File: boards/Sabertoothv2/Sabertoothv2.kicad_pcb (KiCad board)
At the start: 2 copper layers, 45.6 x 45.6 mm, 40 parts, among them J1 Screw_Terminal_01x04, J2 Screw_Terminal_01x04, J4 Conn_01x04_Pin, J5 Conn_01x04_Pin, Q1 NMOS, Q2 NMOS, Q3 NMOS, Q4 NMOS, U1 LM2104, U2 LM2104, U4 74LVC1GU04DRL

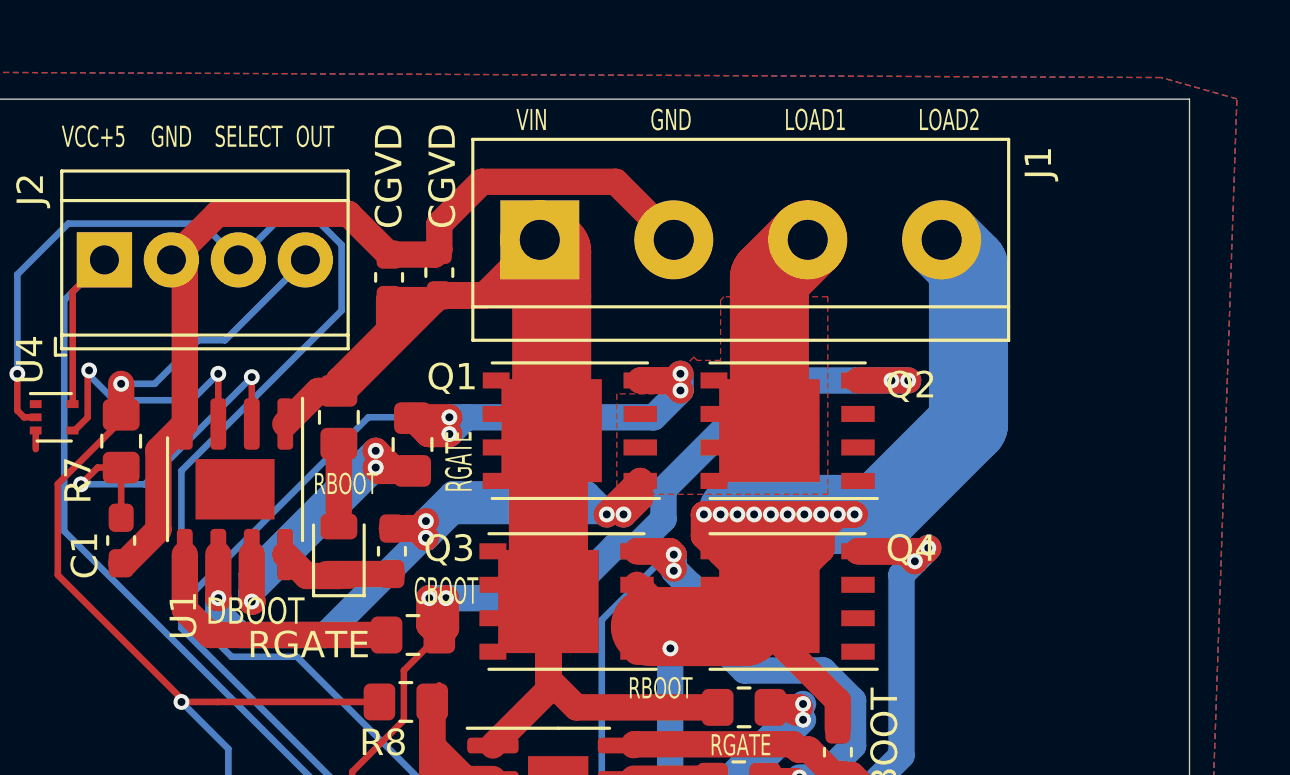
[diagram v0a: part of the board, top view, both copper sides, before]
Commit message: minor changes on front silkscreen and added a smaller iris logo
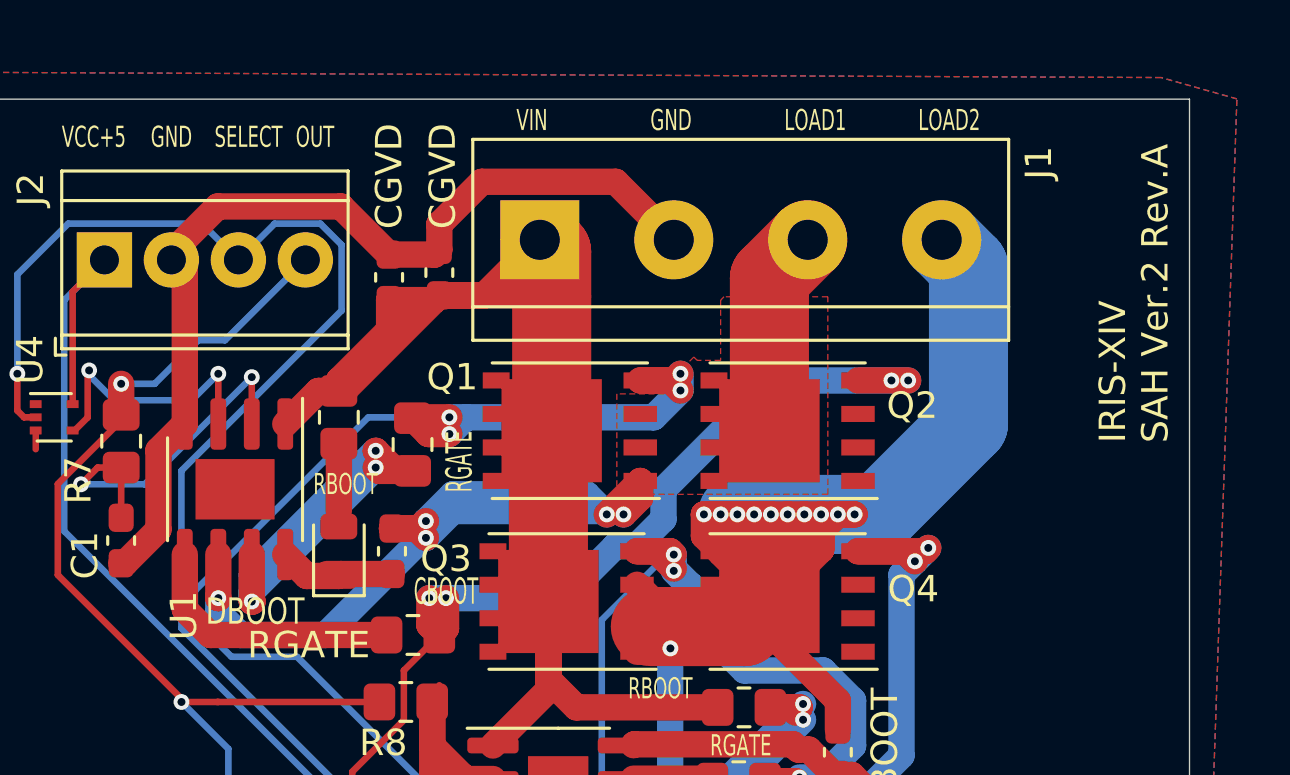
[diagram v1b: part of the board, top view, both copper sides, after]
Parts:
- removed the G*** at (71.1, 40.0)
- added G***: LOGO, Custom_Silkscreen_and_memes:IRIS_logo_smaller, B.Cu at (91.6, 37.5)
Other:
- board text added: "IRIS-XIV SAH Ver.2 Rev.A"
- board text added: "IRIS-XIV SAH Ver.2 Rev.A Buffet Lee, Emily Lory, Joseph Hanger Caroline Chang, Ethan Chang, Jiho Choi, Nathan Colunga, Henry Lin, Ben Saarva, Jashan Virdi, Jakub Wojdyla"
- board text removed: "Nathan Colunga Lee Buffett Emily Lory Joseph Hanger"

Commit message: update name
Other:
- board text added: "IRIS-XIV SAH Ver.2 Rev.A Buffett Lee, Emily Lory, Joseph Hanger Caroline Chang, Ethan Chang, Jiho Choi, Nathan Colunga, Henry Lin, Ben Saarva, Jashan Virdi, Jakub Wojdyla"
- board text removed: "IRIS-XIV SAH Ver.2 Rev.A Buffet Lee, Emily Lory, Joseph Hanger Caroline Chang, Ethan Chang, Jiho Choi, Nathan Colunga, Henry Lin, Ben Saarva, Jashan Virdi, Jakub Wojdyla"
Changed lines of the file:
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@@
     (effects (font (size 1 1) (thickness 0.25) bold) (justify left bottom mirror))
   )
-  (gr_text "IRIS-XIV\nSAH Ver.2 Rev.A\nBuffet Lee, Emily Lory, Joseph Hanger\nCaroline Chang, Ethan Chang, Jiho Choi,\nNathan Colunga, Henry Lin, Ben Saarva, \nJashan Virdi, Jakub Wojdyla" (at 86.49 63.45) (layer "B.SilkS")
+  (gr_text "IRIS-XIV\nSAH Ver.2 Rev.A\nBuffett Lee, Emily Lory, Joseph Hanger\nCaroline Chang, Ethan Chang, Jiho Choi,\nNathan Colunga, Henry Lin, Ben Saarva, \nJashan Virdi, Jakub Wojdyla" (at 86.49 63.45) (layer "B.SilkS")
     (effects (font (size 1 1) (thickness 0.153)) (justify left bottom mirror))
   )

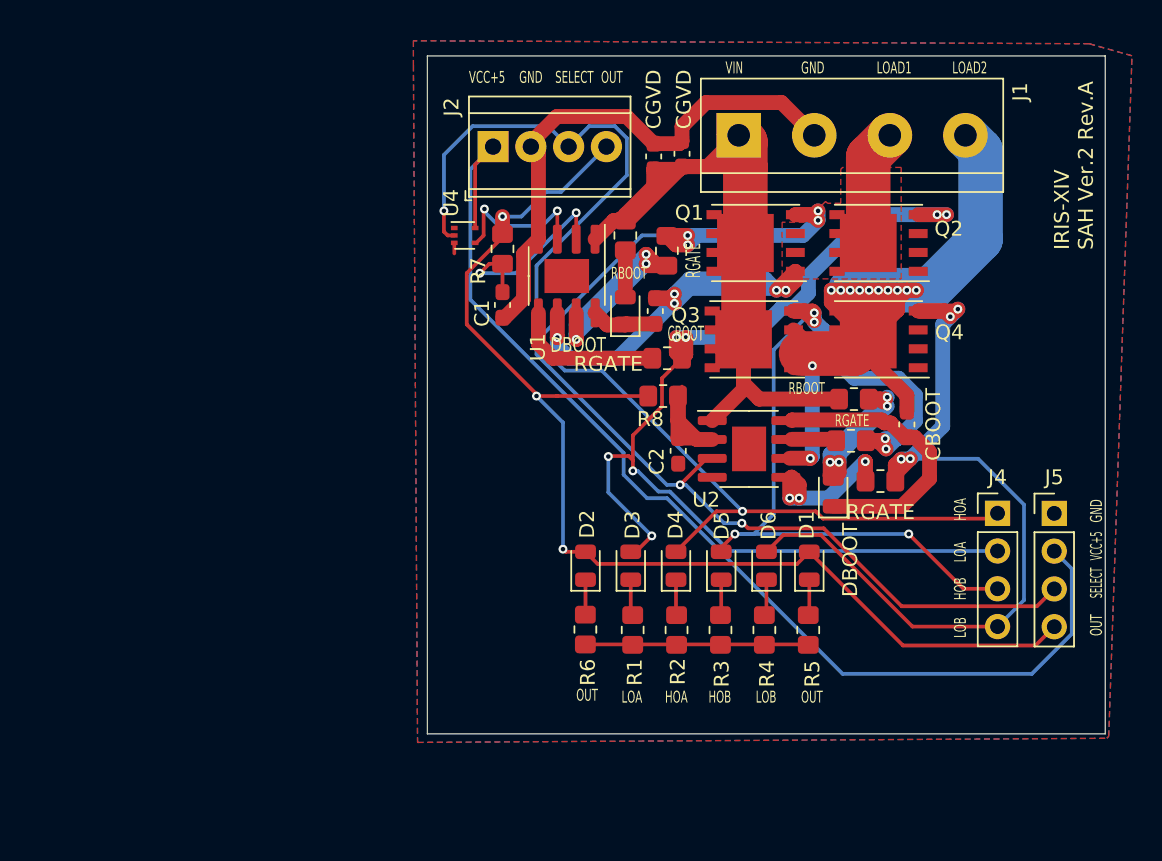
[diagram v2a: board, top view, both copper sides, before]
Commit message: redesigned everything because look better
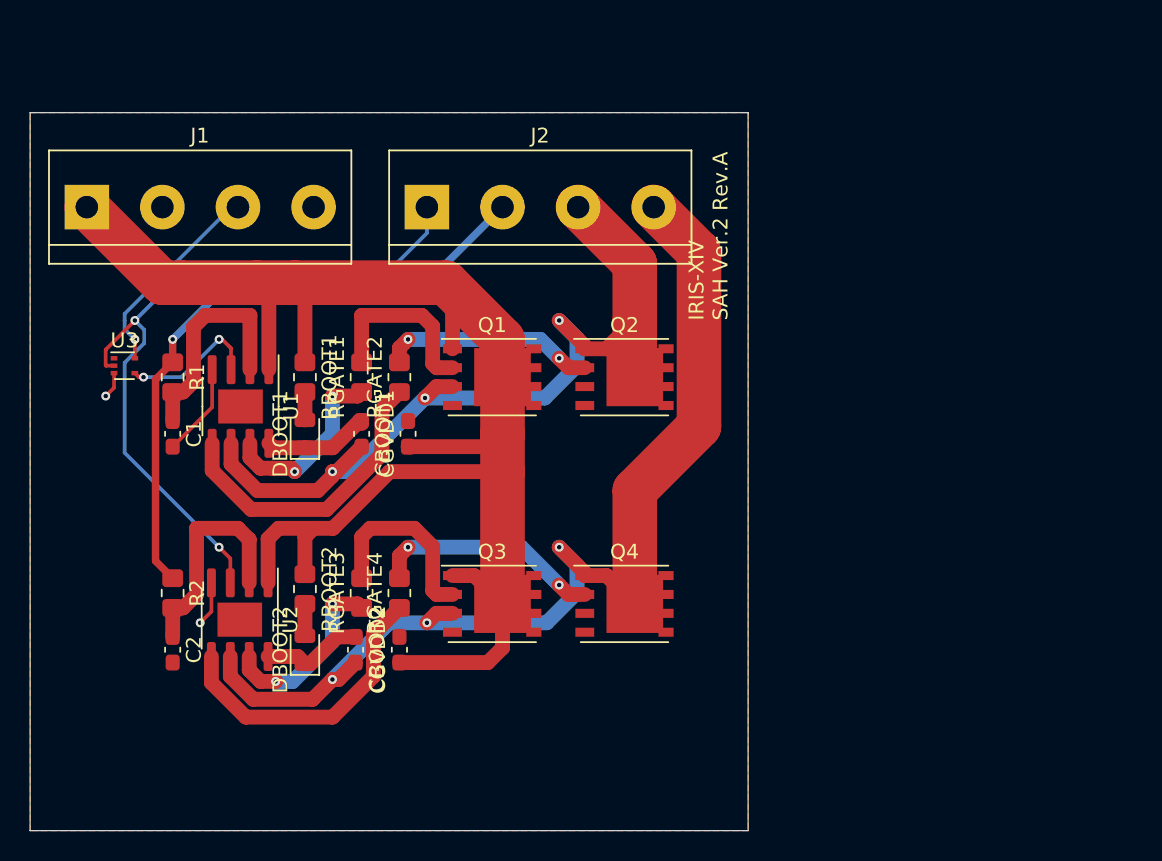
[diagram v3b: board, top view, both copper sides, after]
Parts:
- removed CBOOT (x2): 100nF, Capacitor_SMD:C_0603_1608Metric_Pad1.08x0.95mm_HandSolder
- removed CGVD (x2): 1uF, Capacitor_SMD:C_0603_1608Metric_Pad1.08x0.95mm_HandSolder
- removed D1, D2, D3, D4, D5, D6: LED, LED_SMD:LED_0805_2012Metric
- removed DBOOT (x2): 1V, Diode_SMD:D_0805_2012Metric
- removed J4, J5: Conn_01x04_Pin, Connector_PinHeader_2.54mm:PinHeader_1x04_P2.54mm_Vertical
- removed R3, R4: 1200R, Resistor_SMD:R_0805_2012Metric_Pad1.20x1.40mm_HandSolder
- removed R5, R6: 300R, Resistor_SMD:R_0805_2012Metric_Pad1.20x1.40mm_HandSolder
- removed R7, R8: 50R, Resistor_SMD:R_0805_2012Metric_Pad1.20x1.40mm_HandSolder
- removed RBOOT (x2), RGATE (x4): 2.2R, Resistor_SMD:R_0805_2012Metric_Pad1.20x1.40mm_HandSolder
- removed U4: 74LVC1GU04DRL, Package_TO_SOT_SMD:SOT-553
- added CBOOT1: 100nF, Capacitor_SMD:C_0603_1608Metric_Pad1.08x0.95mm_HandSolder, F.Cu at (46.4, 45.7)
- added CBOOT2: 100nF, Capacitor_SMD:C_0603_1608Metric_Pad1.08x0.95mm_HandSolder, F.Cu at (46.0, 60.2)
- added CGVDD1: 1uF, Capacitor_SMD:C_0603_1608Metric_Pad1.08x0.95mm_HandSolder, F.Cu at (49.5, 45.7)
- added CGVDD2: 1uF, Capacitor_SMD:C_0603_1608Metric_Pad1.08x0.95mm_HandSolder, F.Cu at (49.0, 60.2)
- added DBOOT1: 1V, Diode_SMD:D_0805_2012Metric, F.Cu at (42.6, 45.7)
- added DBOOT2: 1V, Diode_SMD:D_0805_2012Metric, F.Cu at (42.6, 60.2)
- added RBOOT1: 2.2R, Resistor_SMD:R_0805_2012Metric_Pad1.20x1.40mm_HandSolder, F.Cu at (42.6, 41.9)
- added RBOOT2: 2.2R, Resistor_SMD:R_0805_2012Metric_Pad1.20x1.40mm_HandSolder, F.Cu at (42.6, 56.1)
- added RGATE1: 2.2R, Resistor_SMD:R_0805_2012Metric_Pad1.20x1.40mm_HandSolder, F.Cu at (46.4, 41.9)
- added RGATE2: 2.2R, Resistor_SMD:R_0805_2012Metric_Pad1.20x1.40mm_HandSolder, F.Cu at (49.0, 41.9)
- added RGATE3: 2.2R, Resistor_SMD:R_0805_2012Metric_Pad1.20x1.40mm_HandSolder, F.Cu at (46.4, 56.4)
- added RGATE4: 2.2R, Resistor_SMD:R_0805_2012Metric_Pad1.20x1.40mm_HandSolder, F.Cu at (49.0, 56.4)
- added U3: 74LVC1GU04DRL, Package_TO_SOT_SMD:SOT-553, F.Cu at (30.5, 41.1)
- J2: footprint TerminalBlock_TE-Connectivity:TerminalBlock_TE_282834-4_1x04_P2.54mm_Horizontal -> TerminalBlock:TerminalBlock_bornier-4_P5.08mm
- R1, R2: value 1200R -> 50R
- moved J1 44.1 mm to (27.9, 30.5)
- moved C2 36.5 mm to (33.7, 60.2)
- moved U2 36.1 mm to (38.2, 58.2), turned to -90 degrees
- moved R1 35.3 mm to (33.7, 41.9), turned to -90 degrees
- moved R2 34.0 mm to (33.7, 56.4), turned to -90 degrees
- moved G*** 32.9 mm to (67.3, 59.7)
- moved Q3 25.0 mm to (55.2, 57.1), turned to 0 degrees
- moved Q4 24.6 mm to (64.1, 57.1), turned to 0 degrees
- moved C1 23.8 mm to (33.7, 45.7)
- moved U1 23.6 mm to (38.3, 43.9)
- moved Q1 19.9 mm to (55.2, 41.9), turned to 0 degrees
- moved Q2 19.3 mm to (64.1, 41.9), turned to 0 degrees
- moved J2 6.02 mm to (50.8, 30.5)
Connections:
- J1 pad 1: VIN -> VIN+12
- J1 pad 3: LOAD1 -> VIN+5
- J1 pad 4: LOAD2 -> GND
- J2 pad 1: VCC+5 -> SELECT
- J2 pad 2: GND -> PWM
- J2 pad 3: SELECT -> LOAD1
- J2 pad 4: OUT -> LOAD2
- Q1 pad 1: VIN -> VIN+12
- Q3 pad 1: VIN -> VIN+12
- Q3 pad 2: HOB -> HOA
- Q4 pad 2: LOB -> LOA
- R1 pad 1: GND -> PWM
- R1 pad 2: Net-(D3-K) -> Net-(U1-IN)
- R2 pad 1: GND -> PWM
- R2 pad 2: Net-(D4-K) -> Net-(U2-IN)
- U1 pad 1: VIN -> VIN+12
- U2 pad 1: VIN -> VIN+12
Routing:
- net VIN+12: track 0.00 -> 112.5 mm
- net OUT: track 79.6 -> 0.00 mm, vias 3 -> 0
- net VCC+5: track 75.7 -> 0.00 mm
- net HOB: track 61.5 -> 0.00 mm, vias 6 -> 0
- net LOB: track 57.0 -> 0.00 mm, vias 4 -> 0
- net VIN: track 51.1 -> 0.00 mm
- net HOA: track 71.5 -> 24.9 mm, vias 5 -> 0
- net LOA: track 73.3 -> 30.0 mm, vias 7 -> 4
- net PWM: track 0.00 -> 42.9 mm, vias 0 -> 1
- net GND: track 51.9 -> 11.0 mm, vias 0 -> 2
- net SELECT: track 82.9 -> 49.6 mm, vias 3 -> 2
- net LOAD2: track 95.3 -> 72.3 mm, vias 12 -> 3
- net LOAD1: track 42.7 -> 57.4 mm, vias 5 -> 3
- net VIN+5: track 0.00 -> 13.9 mm, vias 0 -> 1
- net Net-(DBOOT2-A): track 15.7 -> 2.14 mm, vias 4 -> 0
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- removed copper zone on B.Cu, net GND
- removed copper zone on F.Cu, net LOAD1
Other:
- board size 45.6 x 45.6 mm -> 48.3 x 48.3 mm
- board text removed: "GND"
- board text removed: "HOA"
- board text removed: "HOB"
- board text removed: "LOA"
- board text removed: "LOAD1"
- board text removed: "LOAD2"
- board text removed: "LOB"
- board text removed: "OUT"
- board text removed: "SELECT"
- board text removed: "VCC+5"
- board text removed: "VIN"

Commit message: added labels for inputs
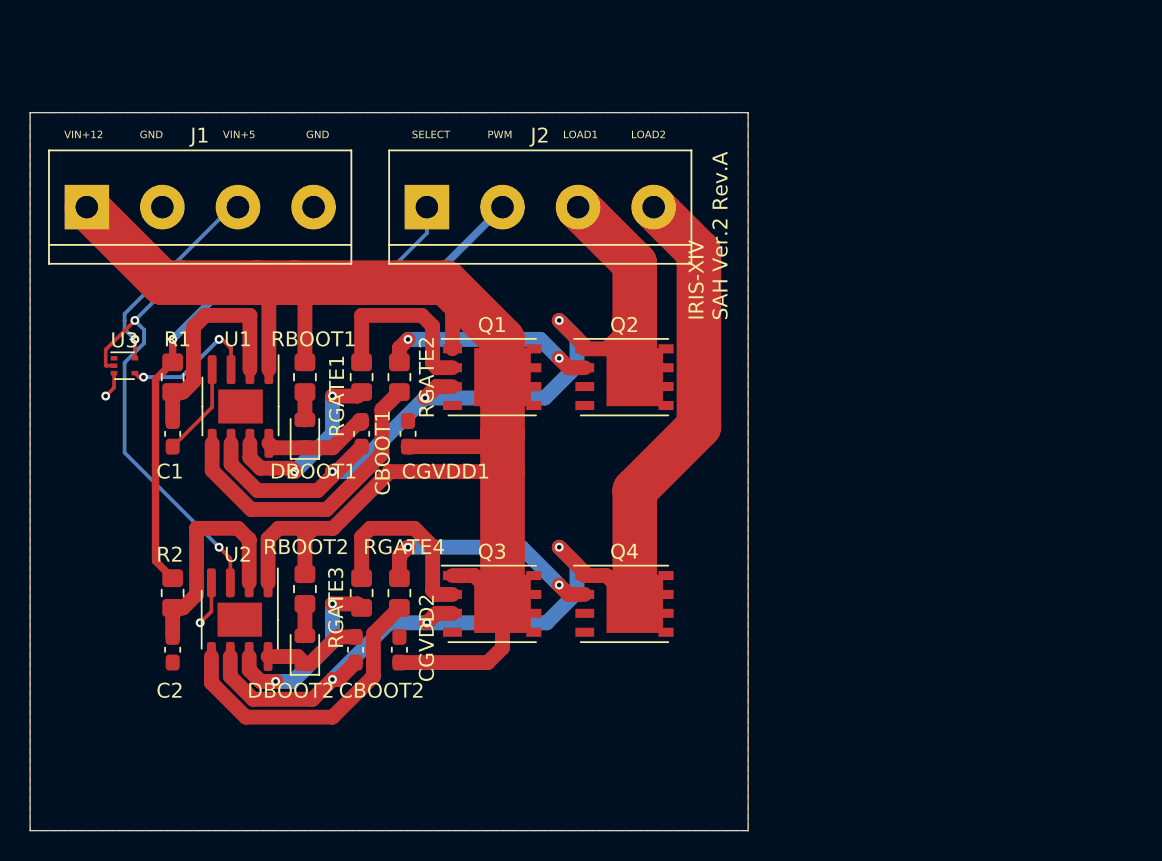
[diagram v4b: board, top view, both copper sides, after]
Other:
- board text added: "GND"
- board text added: "LOAD1"
- board text added: "LOAD2"
- board text added: "PWM"
- board text added: "SELECT"
- board text added: "VIN+12"
- board text added: "VIN+5"
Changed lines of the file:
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@@
     (property "ki_keywords" "cap capacitor")
     (attr smd)
-    (fp_text reference "C1" (at 0 -1.43 90) (layer "F.SilkS")
+    (fp_text reference "C1" (at 2.54 0.182 -180) (layer "F.SilkS")
         (effects (font (size 1 1) (thickness 0.15)))
     )
@@
     (property "ki_keywords" "cap capacitor")
     (attr smd)
-    (fp_text reference "CBOOT1" (at 0 -1.43 90) (layer "F.SilkS")
+    (fp_text reference "CBOOT1" (at 1.27 -1.43 90) (layer "F.SilkS")
         (effects (font (size 1 1) (thickness 0.15)))
     )
@@
     (property "ki_keywords" "driver rs485 rs422 differential")
     (attr smd)
-    (fp_text reference "U2" (at 0 -3.4 90) (layer "F.SilkS")
+    (fp_text reference "U2" (at -4.362 0.12 -180) (layer "F.SilkS")
         (effects (font (size 1 1) (thickness 0.15)))
     )
@@
     (property "ki_keywords" "R res resistor")
     (attr smd)
-    (fp_text reference "RGATE2" (at 0 -1.65 90) (layer "F.SilkS")
+    (fp_text reference "RGATE2" (at 0 1.85 270) (layer "F.SilkS")
         (effects (font (size 1 1) (thickness 0.15)))
     )
@@
     (property "ki_keywords" "R res resistor")
     (attr smd)
-    (fp_text reference "RGATE4" (at 0 -1.65 90) (layer "F.SilkS")
+    (fp_text reference "RGATE4" (at 3.08 0.326 180) (layer "F.SilkS")
         (effects (font (size 1 1) (thickness 0.15)))
     )
@@
     (property "ki_keywords" "diode")
     (attr smd)
-    (fp_text reference "DBOOT2" (at 0 -1.65 90) (layer "F.SilkS")
+    (fp_text reference "DBOOT2" (at -2.762 -0.944 180) (layer "F.SilkS")
         (effects (font (size 1 1) (thickness 0.15)))
     )
@@
     (property "ki_keywords" "R res resistor")
     (attr smd)
-    (fp_text reference "RGATE3" (at 0 -1.65 90) (layer "F.SilkS")
+    (fp_text reference "RGATE3" (at -0.984 -1.706 90) (layer "F.SilkS")
         (effects (font (size 1 1) (thickness 0.15)))
     )
@@
     (property "ki_keywords" "cap capacitor")
     (attr smd)
-    (fp_text reference "CBOOT2" (at 0 -1.43 90) (layer "F.SilkS")
+    (fp_text reference "CBOOT2" (at 2.762 -1.7495 -180) (layer "F.SilkS")
         (effects (font (size 1 1) (thickness 0.15)))
     )
@@
     (property "ki_keywords" "R res resistor")
     (attr smd)
-    (fp_text reference "RBOOT1" (at 0 -1.65 90) (layer "F.SilkS")
+    (fp_text reference "RBOOT1" (at -2.54 -0.58 -180) (layer "F.SilkS")
         (effects (font (size 1 1) (thickness 0.15)))
     )
@@
     (property "ki_keywords" "cap capacitor")
     (attr smd)
-    (fp_text reference "CGVDD1" (at 0 -1.43 90) (layer "F.SilkS")
+    (fp_text reference "CGVDD1" (at -2.54 2.54 180) (layer "F.SilkS")
         (effects (font (size 1 1) (thickness 0.15)))
     )
@@
     (property "ki_keywords" "cap capacitor")
     (attr smd)
-    (fp_text reference "CGVDD2" (at 0 -1.43 90) (layer "F.SilkS")
+    (fp_text reference "CGVDD2" (at 0.794 1.85 90) (layer "F.SilkS")
         (effects (font (size 1 1) (thickness 0.15)))
     )
@@
     (property "ki_keywords" "R res resistor")
     (attr smd)
-    (fp_text reference "R2" (at 0 -1.65 90) (layer "F.SilkS")
+    (fp_text reference "R2" (at -2.572 0.182 -180) (layer "F.SilkS")
         (effects (font (size 1 1) (thickness 0.15)))
     )
@@
     (property "ki_keywords" "diode")
     (attr smd)
-    (fp_text reference "DBOOT1" (at 0 -1.65 90) (layer "F.SilkS")
+    (fp_text reference "DBOOT1" (at -2.54 0.58 180) (layer "F.SilkS")
         (effects (font (size 1 1) (thickness 0.15)))
     )
@@
     (property "ki_keywords" "R res resistor")
     (attr smd)
-    (fp_text reference "RGATE1" (at 0 -1.65 90) (layer "F.SilkS")
+    (fp_text reference "RGATE1" (at -1.27 -1.65 90) (layer "F.SilkS")
         (effects (font (size 1 1) (thickness 0.15)))
     )
@@
     (property "ki_keywords" "R res resistor")
     (attr smd)
-    (fp_text reference "RBOOT2" (at 0 -1.65 90) (layer "F.SilkS")
+    (fp_text reference "RBOOT2" (at -2.81 -0.072 -180) (layer "F.SilkS")
         (effects (font (size 1 1) (thickness 0.15)))
     )
@@
     (property "ki_keywords" "driver rs485 rs422 differential")
     (attr smd)
-    (fp_text reference "U1" (at 0 -3.4 90) (layer "F.SilkS")
+    (fp_text reference "U1" (at -4.51 0.17 -180) (layer "F.SilkS")
         (effects (font (size 1 1) (thickness 0.15)))
     )
@@
     (property "ki_keywords" "R res resistor")
     (attr smd)
-    (fp_text reference "R1" (at 0 -1.65 90) (layer "F.SilkS")
+    (fp_text reference "R1" (at -2.54 -0.326 -180) (layer "F.SilkS")
         (effects (font (size 1 1) (thickness 0.15)))
     )
@@
     (property "ki_keywords" "cap capacitor")
     (attr smd)
-    (fp_text reference "C2" (at 0 -1.43 90) (layer "F.SilkS")
+    (fp_text reference "C2" (at 2.762 0.182 -180) (layer "F.SilkS")
         (effects (font (size 1 1) (thickness 0.15)))
     )
@@
     (effects (font (size 1 1) (thickness 0.153)) (justify left bottom mirror))
   )
+  (gr_text "LOAD1" (at 59.944 25.908) (layer "F.SilkS")
+    (effects (font (size 0.5 0.5) (thickness 0.1)) (justify left bottom))
+  )
+  (gr_text "SELECT" (at 49.784 25.908) (layer "F.SilkS")
+    (effects (font (size 0.5 0.5) (thickness 0.1)) (justify left bottom))
+  )
   (gr_text "IRIS-XIV\nSAH Ver.2 Rev.A" (at 71.12 38.1 90) (layer "F.SilkS")
     (effects (font (size 1 1) (thickness 0.153)) (justify left bottom))
   )
+  (gr_text "VIN+5" (at 37.084 25.908) (layer "F.SilkS")
+    (effects (font (size 0.5 0.5) (thickness 0.1)) (justify left bottom))
+  )
+  (gr_text "GND" (at 31.496 25.908) (layer "F.SilkS")
+    (effects (font (size 0.5 0.5) (thickness 0.1)) (justify left bottom))
+  )
+  (gr_text "VIN+12" (at 26.416 25.908) (layer "F.SilkS")
+    (effects (font (size 0.5 0.5) (thickness 0.1)) (justify left bottom))
+  )
+  (gr_text "LOAD2" (at 64.516 25.908) (layer "F.SilkS")
+    (effects (font (size 0.5 0.5) (thickness 0.1)) (justify left bottom))
+  )
+  (gr_text "PWM" (at 54.864 25.908) (layer "F.SilkS")
+    (effects (font (size 0.5 0.5) (thickness 0.1)) (justify left bottom))
+  )
+  (gr_text "GND" (at 42.672 25.908) (layer "F.SilkS")
+    (effects (font (size 0.5 0.5) (thickness 0.1)) (justify left bottom))
+  )
   (segment (start 35.9 37.76) (end 35.11 38.55) (width 1) (layer "F.Cu") (net 1))
